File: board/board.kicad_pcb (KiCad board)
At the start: 4 copper layers, 36.4 x 18 mm, 20 parts, among them J1 022_battery_cells, J2 011_GPIO, U1 LM2623LDX/NOPB

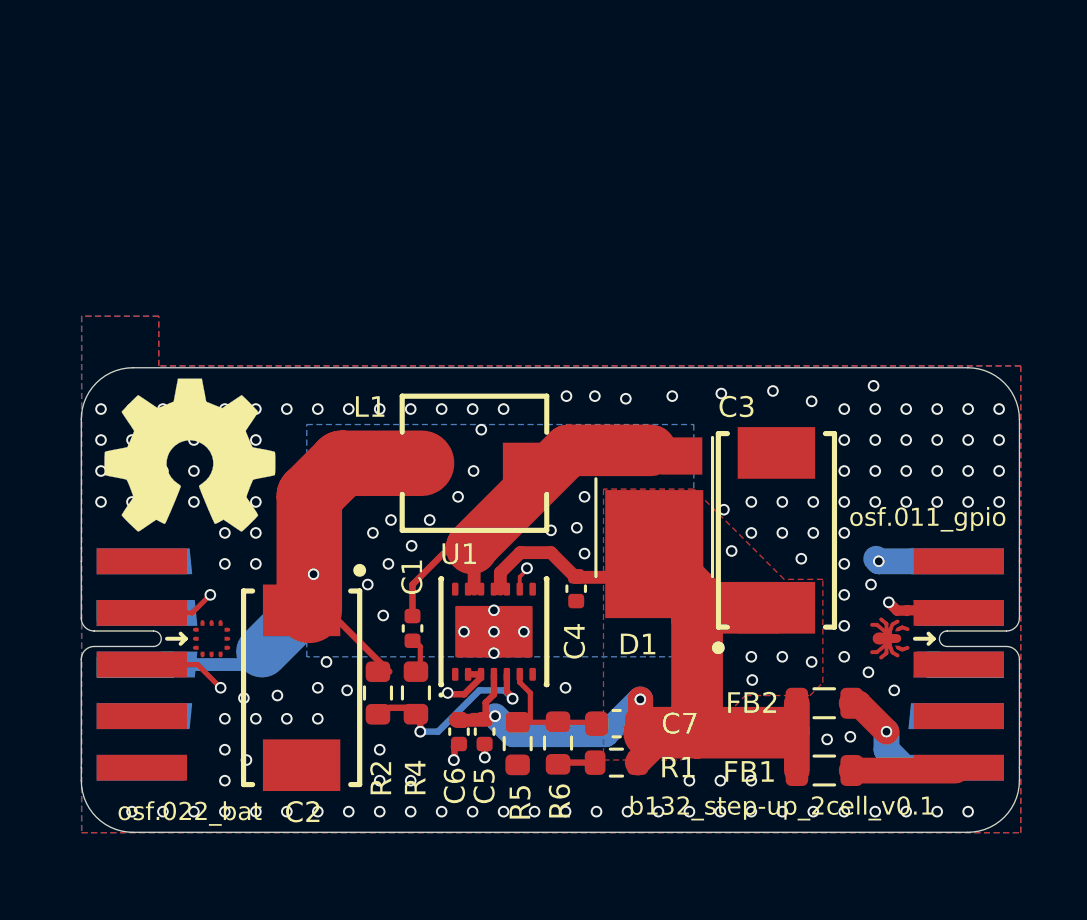
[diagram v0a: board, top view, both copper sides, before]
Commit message: switched edge connectors to use the correct footprints and renamed local libraries to fit with the edgy naming convention
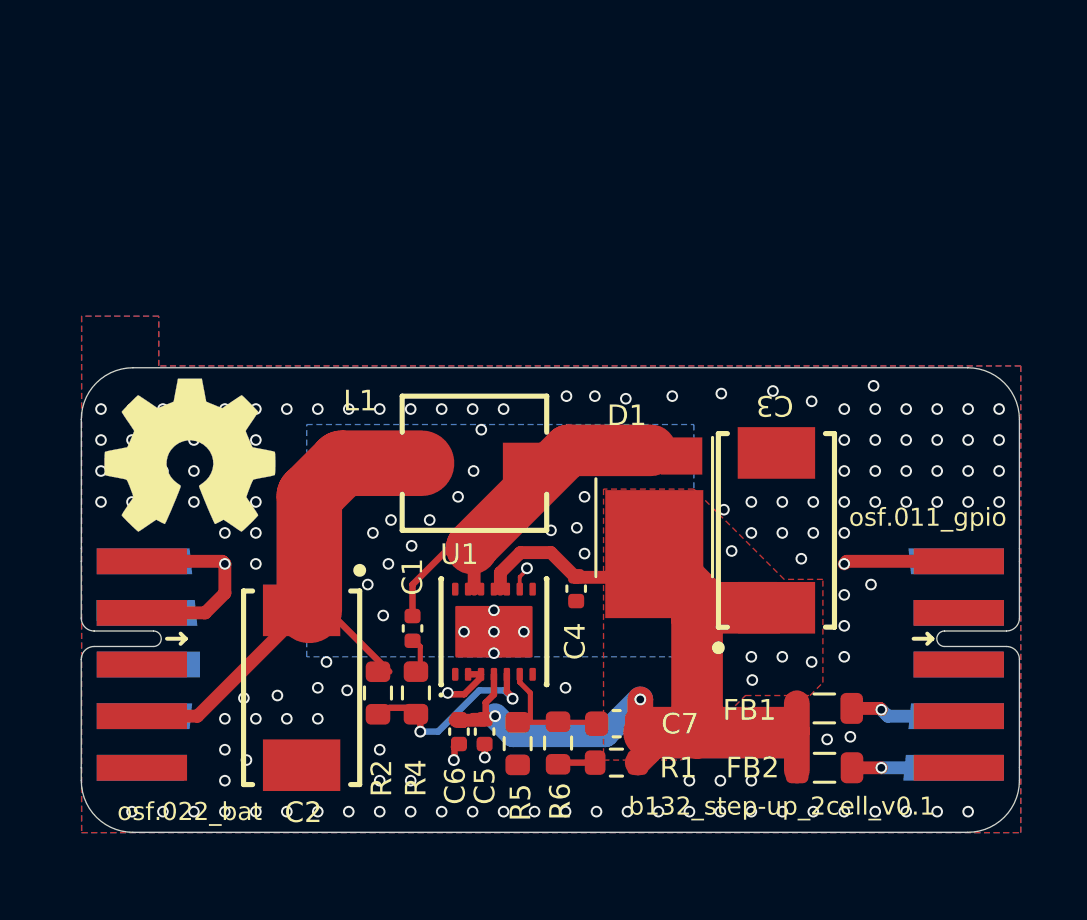
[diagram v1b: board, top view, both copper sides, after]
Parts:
- C2, C3: footprint stpup:CAPMP7344X43-T_V -> b132:CAPMP7344X43-T_V
- D1: footprint stpup:PMEG100V100ELPDAZ -> b132:PMEG100V100ELPDAZ
- J1: footprint on_edge:debug_edge_2x05_device -> on_edge:on_edge_2x05_device
- J2: footprint on_edge:debug_edge_2x05_host -> on_edge:on_edge_2x05_host
- L1: footprint stpup:WURTH 5040 -> b132:WURTH 5040
- U1: footprint stpup:NHE0014A_V -> b132:NHE0014A_V
- moved FB2 2.50 mm to (168.8, 100.5)
- moved FB1 2.41 mm to (168.8, 98.2)
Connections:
- J2 pad 8: GND -> unconnected-(J2-Pad8)
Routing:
- net /stepup_2-LR6/VIN: track 22.4 -> 21.4 mm, vias 1 -> 0
- net /stepup_2-LR6/5V: track 3.35 -> 3.99 mm
- net GND: vias 160 -> 154
- net /stepup_2-LR6/3.3V: track 4.19 -> 4.22 mm, vias 0 -> 1

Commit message: changed constraints to work as a 2 layer board, changed symbols to kicad native
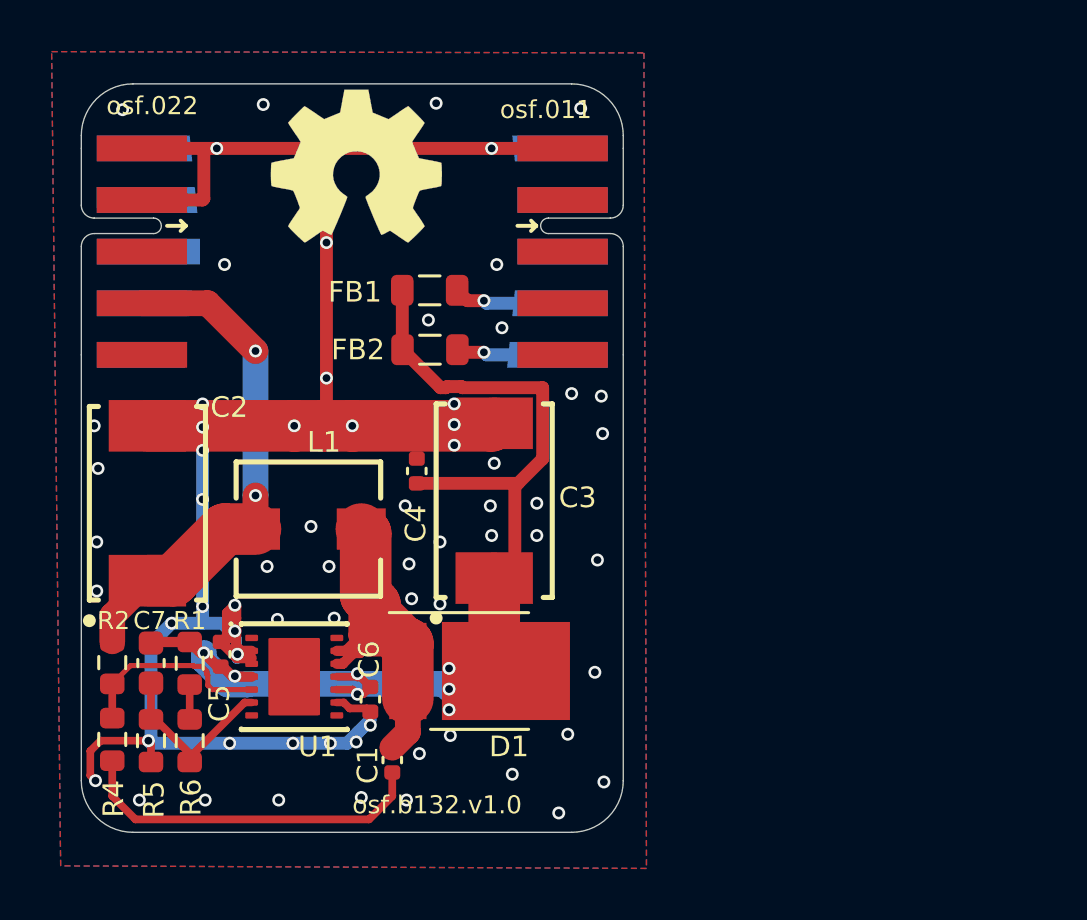
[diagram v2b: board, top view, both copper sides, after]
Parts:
- R2: value 75 kOhms -> 75R
- moved FB2 22.3 mm to (153.5, 84.3)
- moved FB1 22.3 mm to (153.5, 82.0)
- moved J2 22.2 mm to (161.0, 80.5)
- moved C7 18.2 mm to (142.7, 96.4), turned to -90 degrees
- moved R1 17.0 mm to (144.2, 96.5), turned to 90 degrees
- moved J1 16.0 mm to (140.0, 80.5)
- moved R6 14.3 mm to (144.2, 99.5), turned to 90 degrees
- moved R5 14.2 mm to (142.7, 99.5)
- moved LOGO1 12.9 mm to (150.7, 77.2)
- moved R4 11.9 mm to (141.2, 99.4), turned to -90 degrees
- moved C3 11.0 mm to (156.0, 90.2)
- moved C5 10.7 mm to (145.4, 96.1)
- moved R2 10.4 mm to (141.2, 96.4), turned to 90 degrees
- moved C2 9.32 mm to (142.6, 90.2), turned to 90 degrees
- moved U1 7.93 mm to (148.2, 97.0), turned to 0 degrees
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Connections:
- C1 pad 1: Net-(C1-Pad1) -> /stepup_2-LR6/SW
- C1 pad 2: /stepup_2-LR6/SW -> Net-(C1-Pad2)
- C4 pad 1: GND -> /stepup_2-LR6/VDD
- C4 pad 2: /stepup_2-LR6/VDD -> GND
- C5 pad 1: GND -> /stepup_2-LR6/VDD
- C5 pad 2: /stepup_2-LR6/VDD -> GND
- C6 pad 1: GND -> /stepup_2-LR6/VDD
- C6 pad 2: /stepup_2-LR6/VDD -> GND
- R2 pad 1: /stepup_2-LR6/VIN -> /stepup_2-LR6/FREQ
- R2 pad 2: /stepup_2-LR6/FREQ -> /stepup_2-LR6/VIN
- R4 pad 2: Net-(C1-Pad1) -> Net-(C1-Pad2)
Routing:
- net GND: track 16.3 -> 83.9 mm, vias 154 -> 68
- net Net-(C1-Pad2): track 0.00 -> 13.9 mm
- net /stepup_2-LR6/SW: track 15.1 -> 18.4 mm
- net /stepup_2-LR6/VDD: track 41.3 -> 43.5 mm, vias 2 -> 7
- net /stepup_2-LR6/FB: track 5.58 -> 7.21 mm
- net Net-(C1-Pad1): track 1.49 -> 0.00 mm
- net /stepup_2-LR6/VIN: track 21.4 -> 20.0 mm, vias 0 -> 2
- net /stepup_2-LR6/FREQ: track 7.54 -> 7.70 mm, vias 2 -> 0
- net /stepup_2-LR6/HEATSINK: vias 5 -> 0
- removed copper zone on B.Cu, net /stepup_2-LR6/HEATSINK
- removed copper zone on In1.Cu, net GND
- removed copper zone on In2.Cu, net GND
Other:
- board size 36.4 x 18 mm -> 21 x 29 mm
- copper layers 4 -> 2
- board text added: "osf.011"
- board text added: "osf.022"
- board text added: "osf.b132.v1.0"
- board text removed: "b132_step-up_2cell_v0.1"
- board text removed: "osf.011_gpio"
- board text removed: "osf.022_bat"

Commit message: switched to ceramic caps
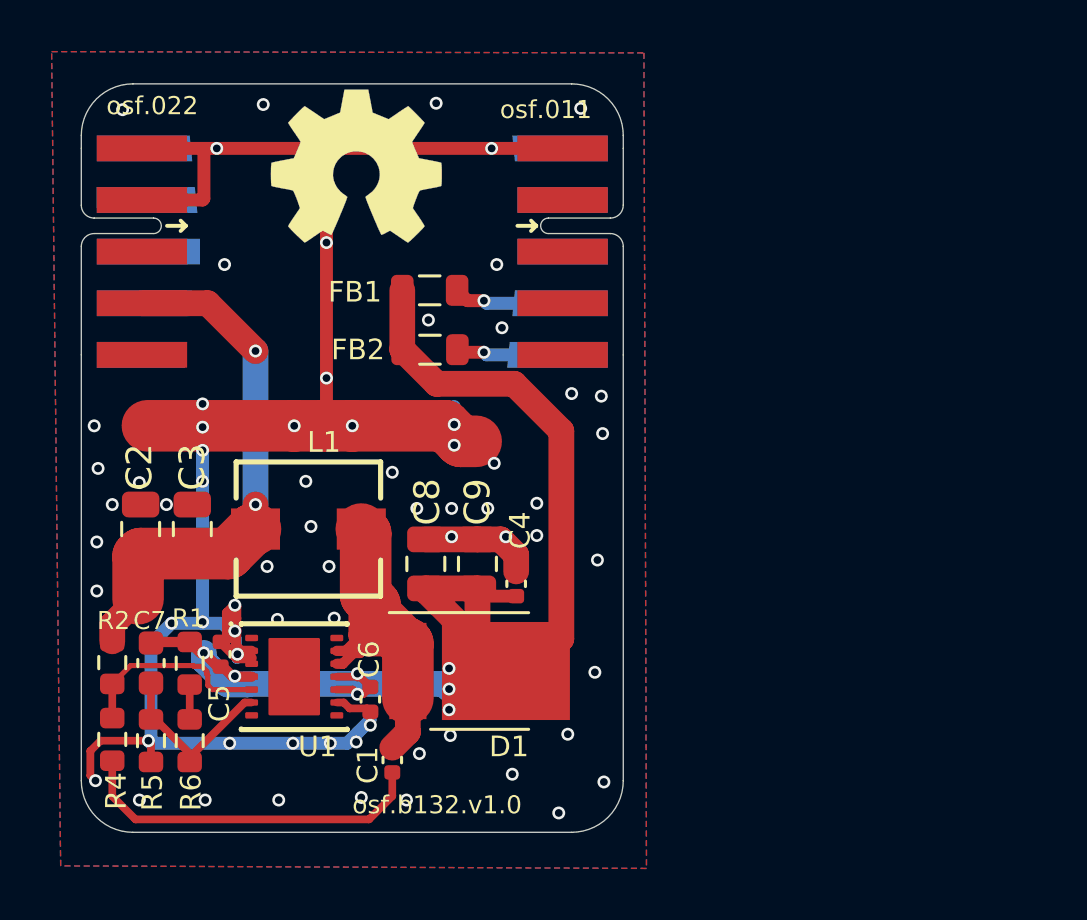
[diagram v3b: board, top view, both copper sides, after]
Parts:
- added C8: 22uF, Capacitor_SMD:C_0805_2012Metric, F.Cu at (153.3, 92.6)
- added C9: 22uF, Capacitor_SMD:C_0805_2012Metric, F.Cu at (155.3, 92.6)
- C2, C3: value TPSE107K016R0100 -> 22uF; footprint b132:CAPMP7344X43-T_V -> Capacitor_SMD:C_0805_2012Metric
- moved C3 11.8 mm to (144.3, 91.2)
- moved C4 5.82 mm to (156.8, 93.4)
- moved C2 1.03 mm to (142.3, 91.2)
- turned R1 to -90 degrees
- turned R4 to 90 degrees
- turned R5 to -90 degrees
- turned R6 to -90 degrees
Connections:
- C1 pad 2: Net-(C1-Pad2) -> Net-(R4-Pad1)
- C3 pad 1: /stepup_2-LR6/VDD -> /stepup_2-LR6/VIN
- R1 pad 1: Net-(R1-Pad1) -> /stepup_2-LR6/VDD
- R1 pad 2: /stepup_2-LR6/VDD -> Net-(R1-Pad2)
- R4 pad 1: /stepup_2-LR6/FREQ -> Net-(R4-Pad1)
- R4 pad 2: Net-(C1-Pad2) -> /stepup_2-LR6/FREQ
- R5 pad 1: GND -> /stepup_2-LR6/FB
- R5 pad 2: /stepup_2-LR6/FB -> GND
- R6 pad 1: /stepup_2-LR6/FB -> Net-(R1-Pad2)
- R6 pad 2: Net-(R1-Pad1) -> /stepup_2-LR6/FB
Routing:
- net Net-(R4-Pad1): track 0.00 -> 13.9 mm
- net Net-(C1-Pad2): track 13.9 -> 0.00 mm
- net /stepup_2-LR6/VDD: track 43.5 -> 51.5 mm
- net GND: track 83.9 -> 87.8 mm, vias 68 -> 70
- net Net-(R1-Pad2): track 0.00 -> 1.35 mm
- net Net-(R1-Pad1): track 1.35 -> 0.00 mm
- net /stepup_2-LR6/VIN: track 20.0 -> 20.8 mm
